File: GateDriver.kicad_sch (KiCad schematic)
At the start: 15 parts, among them U7 2ED4820EMXUMA2

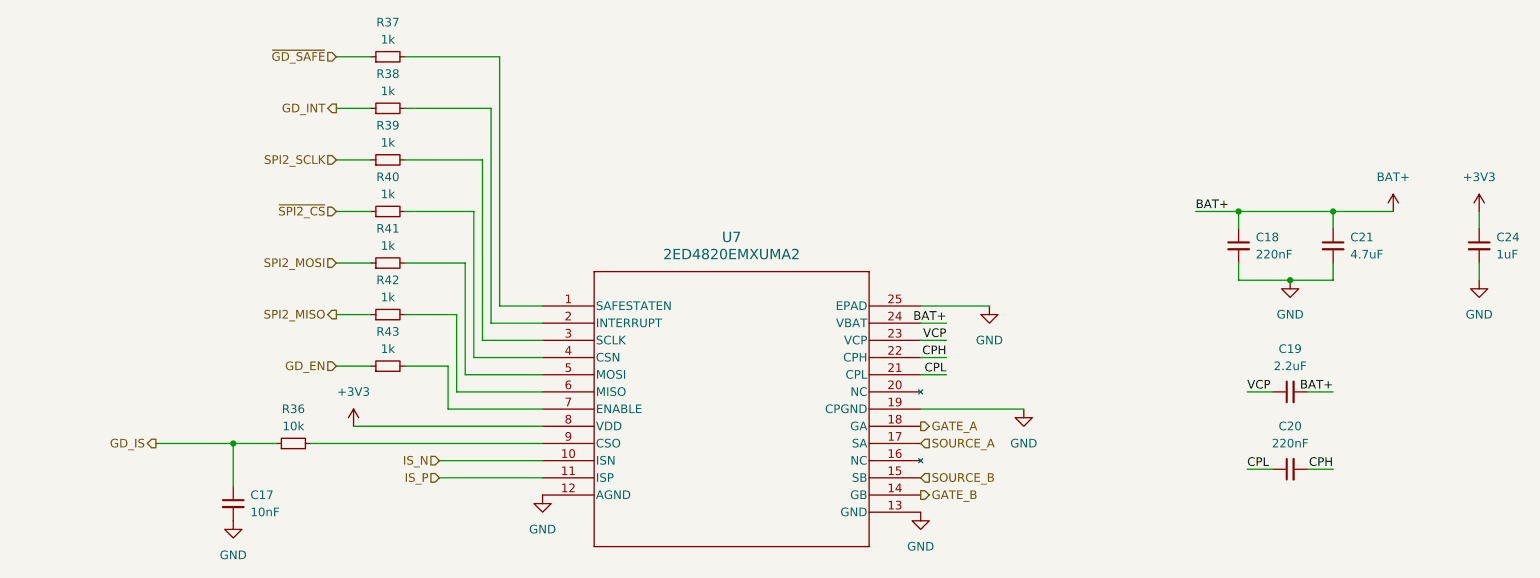
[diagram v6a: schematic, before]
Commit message: More routing, changed the footprints of some caps.
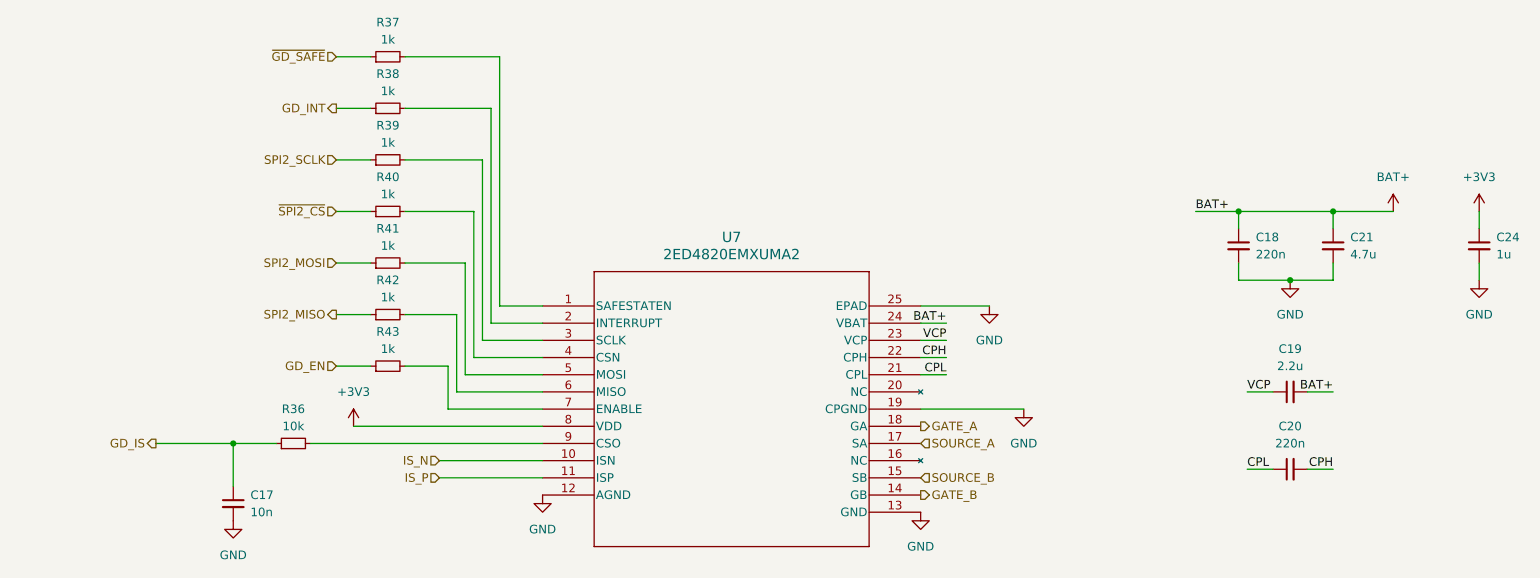
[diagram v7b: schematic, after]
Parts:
- C17: value 10nF -> 10n
- C18, C20: value 220nF -> 220n; footprint Capacitor_SMD:C_0603_1608Metric -> Capacitor_SMD:C_1206_3216Metric
- C19: value 2.2uF -> 2.2u; footprint Capacitor_SMD:C_0603_1608Metric -> Capacitor_SMD:C_1206_3216Metric
- C21: value 4.7uF -> 4.7u; footprint Capacitor_SMD:C_0603_1608Metric -> Capacitor_SMD:C_1206_3216Metric
- C24: value 1uF -> 1u
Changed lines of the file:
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@@
 			)
 		)
-		(property "Value" "220nF"
+		(property "Value" "220n"
 			(at 257.8163 104.14 90)
 			(effects
@@
 			)
 		)
-		(property "Footprint" "Capacitor_SMD:C_0603_1608Metric"
+		(property "Footprint" "Capacitor_SMD:C_1206_3216Metric"
 			(at 257.81 107.95 0)
 			(effects
@@
 			)
 		)
-		(property "Value" "10nF"
+		(property "Value" "10n"
 			(at 104.14 114.3062 0)
 			(effects
@@
 			)
 		)
-		(property "Value" "4.7uF"
+		(property "Value" "4.7u"
 			(at 266.7 76.2062 0)
 			(effects
@@
 			)
 		)
-		(property "Footprint" "Capacitor_SMD:C_0603_1608Metric"
+		(property "Footprint" "Capacitor_SMD:C_1206_3216Metric"
 			(at 264.16 74.93 0)
 			(effects
@@
 			)
 		)
-		(property "Value" "2.2uF"
+		(property "Value" "2.2u"
 			(at 257.8163 92.71 90)
 			(effects
@@
 			)
 		)
-		(property "Footprint" "Capacitor_SMD:C_0603_1608Metric"
+		(property "Footprint" "Capacitor_SMD:C_1206_3216Metric"
 			(at 257.81 96.52 0)
 			(effects
@@
 			)
 		)
-		(property "Value" "1uF"
+		(property "Value" "1u"
 			(at 288.29 76.2062 0)
 			(effects
@@
 			)
 		)
-		(property "Value" "220nF"
+		(property "Value" "220n"
 			(at 252.73 76.2062 0)
 			(effects
@@
 			)
 		)
-		(property "Footprint" "Capacitor_SMD:C_0603_1608Metric"
+		(property "Footprint" "Capacitor_SMD:C_1206_3216Metric"
 			(at 250.19 74.93 0)
 			(effects

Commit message: add manufacturer, mpn, and package to bom
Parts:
- C17: Manufacturer_Name (none) -> Murata Electronics; Manufacturer_Part_Number (none) -> GCM188R72A103KA37D; Package (none) -> 603
- C18, C20: Manufacturer_Name (none) -> TDK Corporation; Manufacturer_Part_Number (none) -> C3216X7R2A224K115AA; Package (none) -> 1206
- C19: Manufacturer_Name (none) -> Samsung Electro-Mechanics; Manufacturer_Part_Number (none) -> CL31B225KCHSNNE; Package (none) -> 1206
- C21: Manufacturer_Name (none) -> Murata Electronics; Manufacturer_Part_Number (none) -> GRM31CC72A475KE11L; Package (none) -> 1206
- C24: Manufacturer_Name (none) -> Taiyo Yuden; Manufacturer_Part_Number (none) -> TMK107B7105KA-T; Package (none) -> 603
- R36: Manufacturer_Name (none) -> YAGEO; Manufacturer_Part_Number (none) -> RC0603JR-0710KL; Package (none) -> 603
- R37, R38, R39, R40, R41, R42, R43: Manufacturer_Name (none) -> YAGEO; Manufacturer_Part_Number (none) -> RC0603FR-071KL; Package (none) -> 603
- U7: Manufacturer_Name (none) -> Infineon Technologies; Manufacturer_Part_Number (none) -> 2ED4820EMXUMA2; Package (none) -> PG-TSDSO-24
